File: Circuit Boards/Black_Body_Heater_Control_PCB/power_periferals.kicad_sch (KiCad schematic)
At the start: 32 parts, among them P301 436500200, P302 436500200, Q302 BD139, U301 DAC60501ZDGSR, U302 INA181A2IDBVR, U304 LMR51420XFDDCR, U305 LM358

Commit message: Minor pcb changes
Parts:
- removed C302, C303, C304: 1uf, Capacitor_SMD:C_0603_1608Metric, symbol Device:C
- removed C305, C306: 100nf, Capacitor_SMD:C_0603_1608Metric, symbol Device:C
- removed C307, C308, C309: 10uf, Capacitor_SMD:C_0603_1608Metric, symbol Device:C
- removed L301: SRR1208-120ML, -inductors:SRR1208, symbol Device:L
- removed R309: 162k, Resistor_SMD:R_0603_1608Metric, symbol Device:R
- removed R310: 22.6k, Resistor_SMD:R_0603_1608Metric, symbol Device:R
- removed U304: LMR51420XFDDCR, Package_TO_SOT_SMD:SOT-23-6, symbol Regulator_Switching:LMR51430
- added U303: (no value), -buck:TPSM84209, symbol -buck:TPSM84209RKHR
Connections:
- net i2c.scl: now also U301.7 (~{SYNC}/A0)
- new net: U303.6 (NC), U303.7 (NC)
- no-connect marks 5 -> 4
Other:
- note added: "https://webench.ti.com/appinfo/webench/scripts/SDP.cgi?ID=98AC47456104FA3F"
- note removed: "https://webench.ti.com/appinfo/webench/scripts/SDP.cgi?ID=251D6F2279A1AAEF"

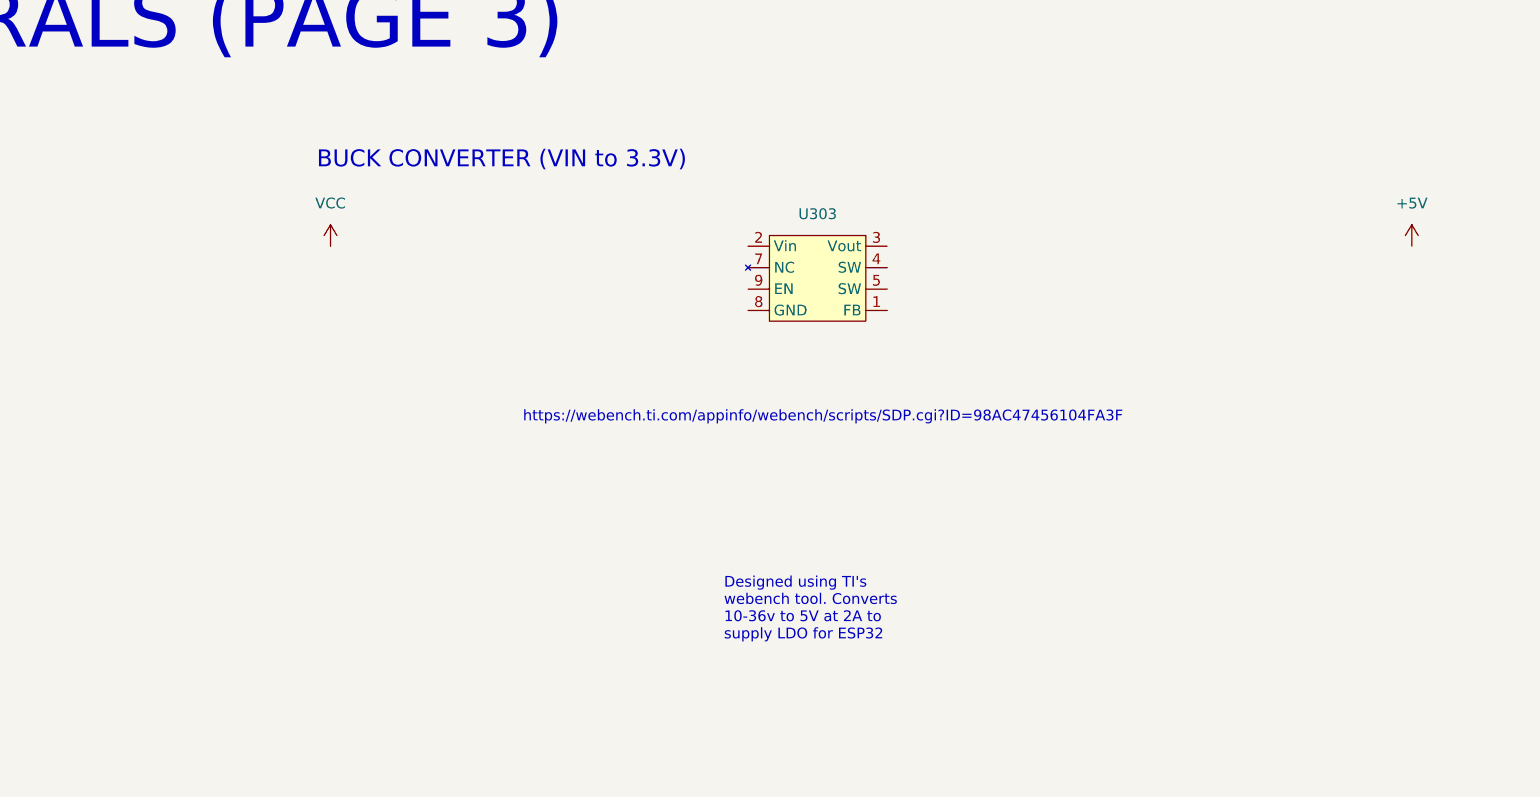
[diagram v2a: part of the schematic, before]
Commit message: Required Schematic changes made
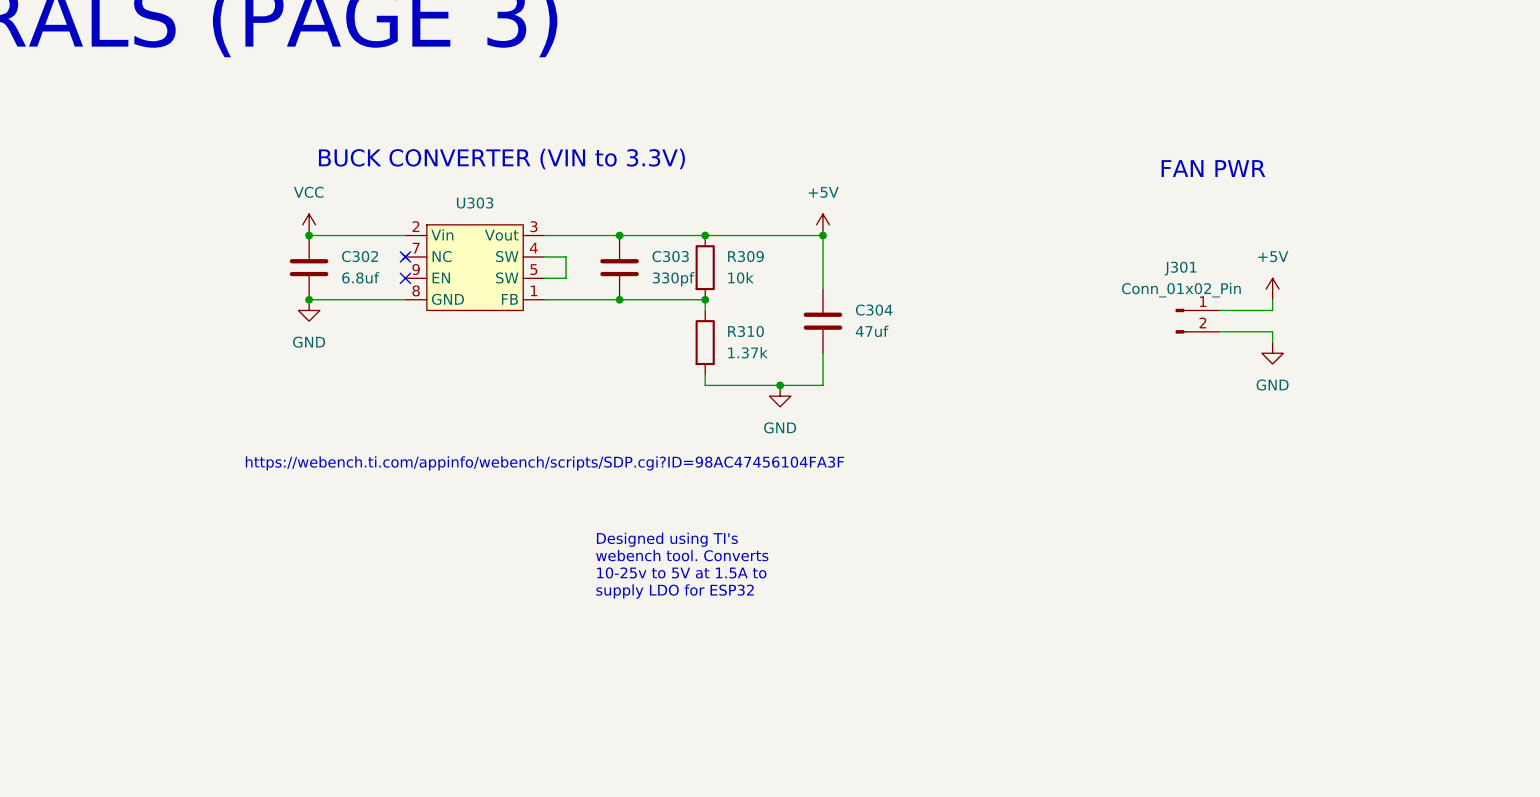
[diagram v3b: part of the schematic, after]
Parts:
- added C302: 6.8uf, Capacitor_SMD:C_0603_1608Metric, symbol Device:C
- added C303: 330pf, Capacitor_SMD:C_0603_1608Metric, symbol Device:C
- added C304: 47uf, Capacitor_SMD:C_1210_3225Metric, symbol Device:C
- added J301: Conn_01x02_Pin, Connector_PinHeader_1.27mm:PinHeader_1x02_P1.27mm_Vertical, symbol Connector:Conn_01x02_Pin
- added R309: 10k, Resistor_SMD:R_0603_1608Metric, symbol Device:R
- added R310: 1.37k, Resistor_SMD:R_0603_1608Metric, symbol Device:R
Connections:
- net +5V: now also U303.3 (Vout), C303.1, C304.1, J301.1 (Pin_1), R309.1
- net GND: now also U303.8 (GND), C302.2, C304.2, J301.2 (Pin_2), R310.2
- net VCC: now also U303.2 (Vin), C302.1
- net at U303.1 (FB): now also C303.2, R309.2, R310.1
- net at U303.4 (SW): now also U303.5 (SW)
- no-connect marks 4 -> 6
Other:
- note added: "FAN PWR"
- moved on the sheet: U303

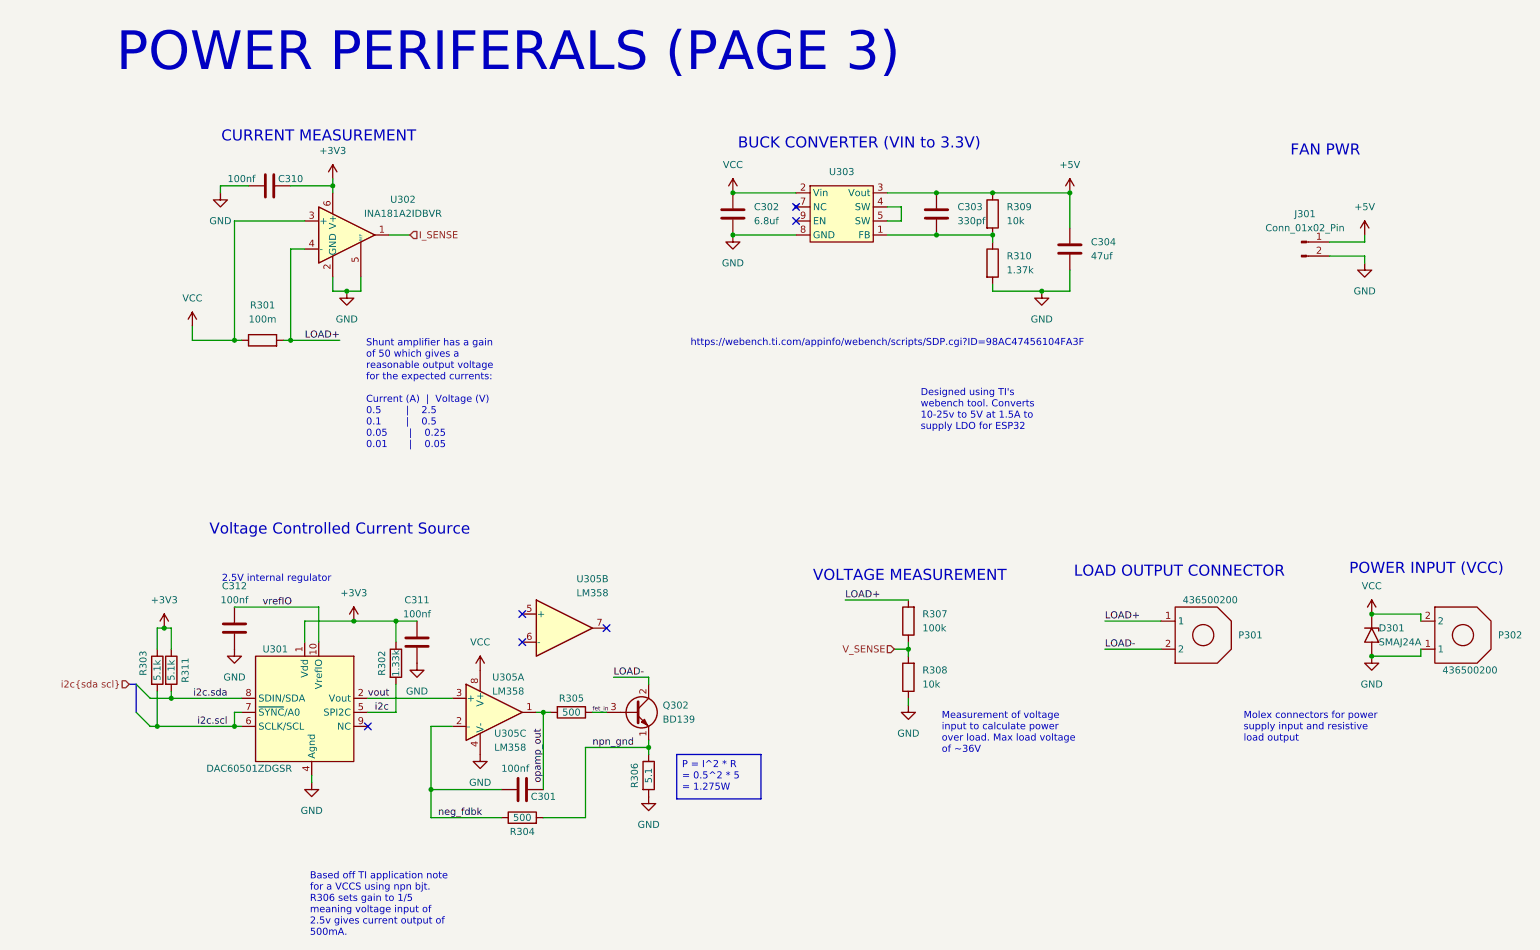
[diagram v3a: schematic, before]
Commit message: Changing buck on heater pcb
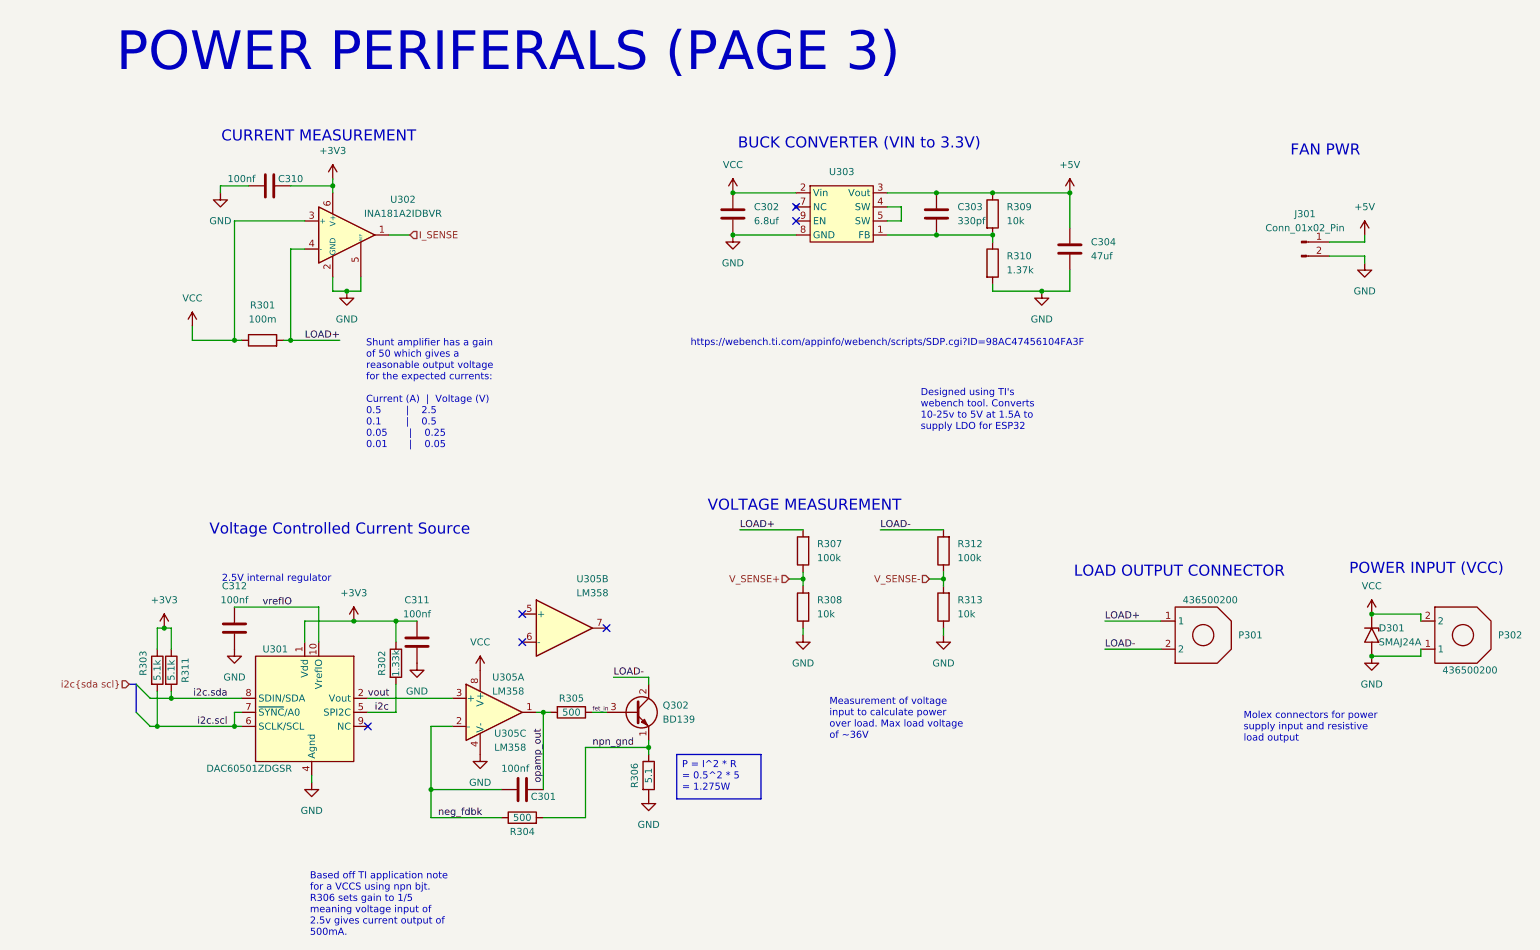
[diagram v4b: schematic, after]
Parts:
- added R312: 100k, Resistor_SMD:R_0603_1608Metric, symbol Device:R
- added R313: 10k, Resistor_SMD:R_0603_1608Metric, symbol Device:R
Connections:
- net GND: now also R313.1
- net LOAD-: now also R312.2
- net V_SENSE renamed V_SENSE+
- new net V_SENSE-: R312.1, R313.2
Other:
- moved on the sheet: R307, R308
